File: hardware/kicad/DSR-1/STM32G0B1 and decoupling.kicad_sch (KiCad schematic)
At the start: 0 parts

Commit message: Refactor code structure for improved readability and maintainability
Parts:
- added U5: STM32G0B1KBUx, Package_DFN_QFN:QFN-32-1EP_5x5mm_P0.5mm_EP3.45x3.45mm, symbol DSR-1:STM32G0B1KBUx
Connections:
- net +3.3V: now also U5.1 (PB9), U5.31 (PB7), U5.4 (VDD)
- net GND: now also U5.16 (PB1), U5.17 (PB2), U5.33 (VSS), U5.5 (VSS)

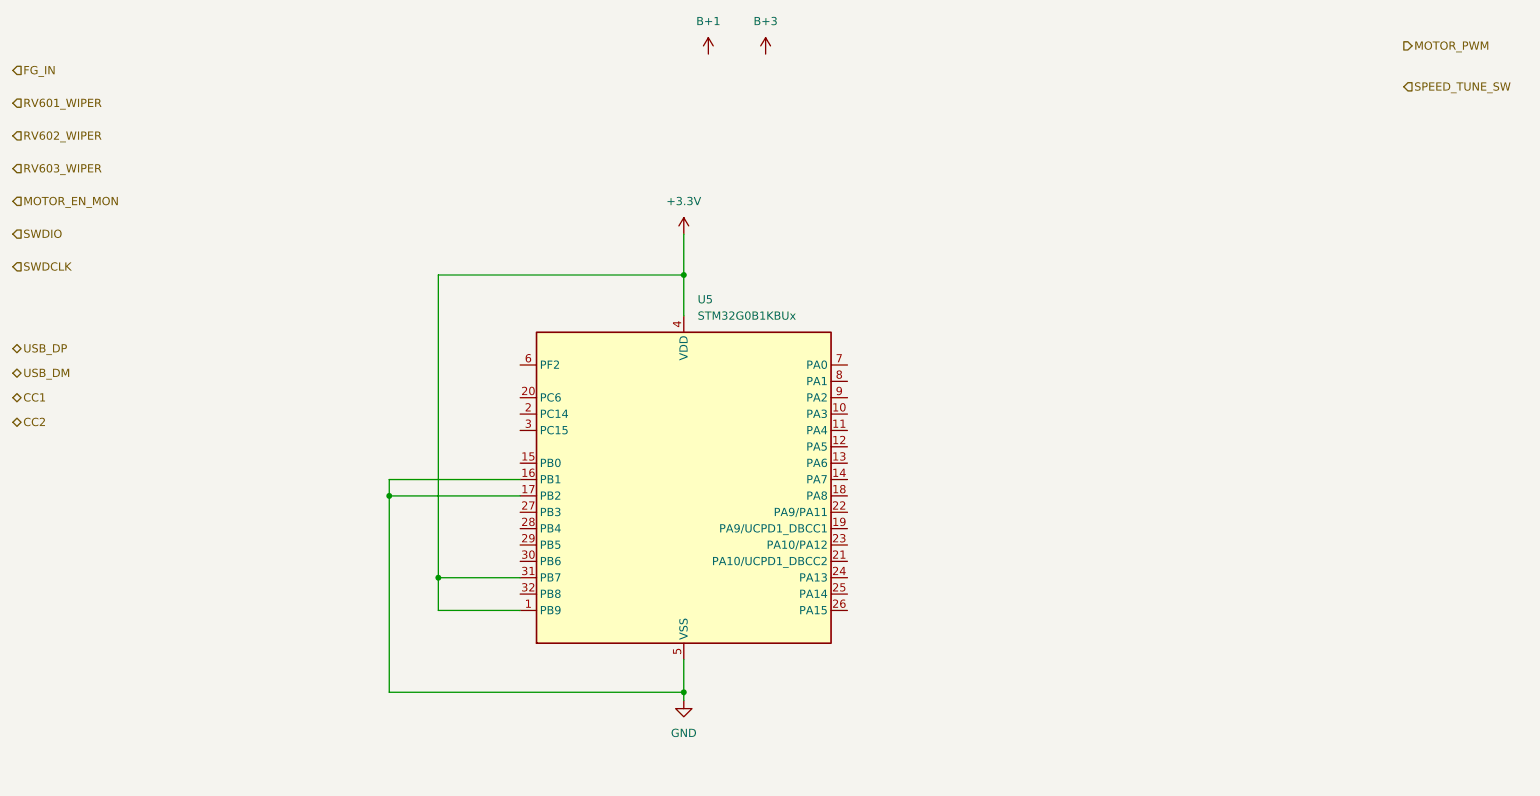
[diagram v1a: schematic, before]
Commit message: Completed microcontroller schematic
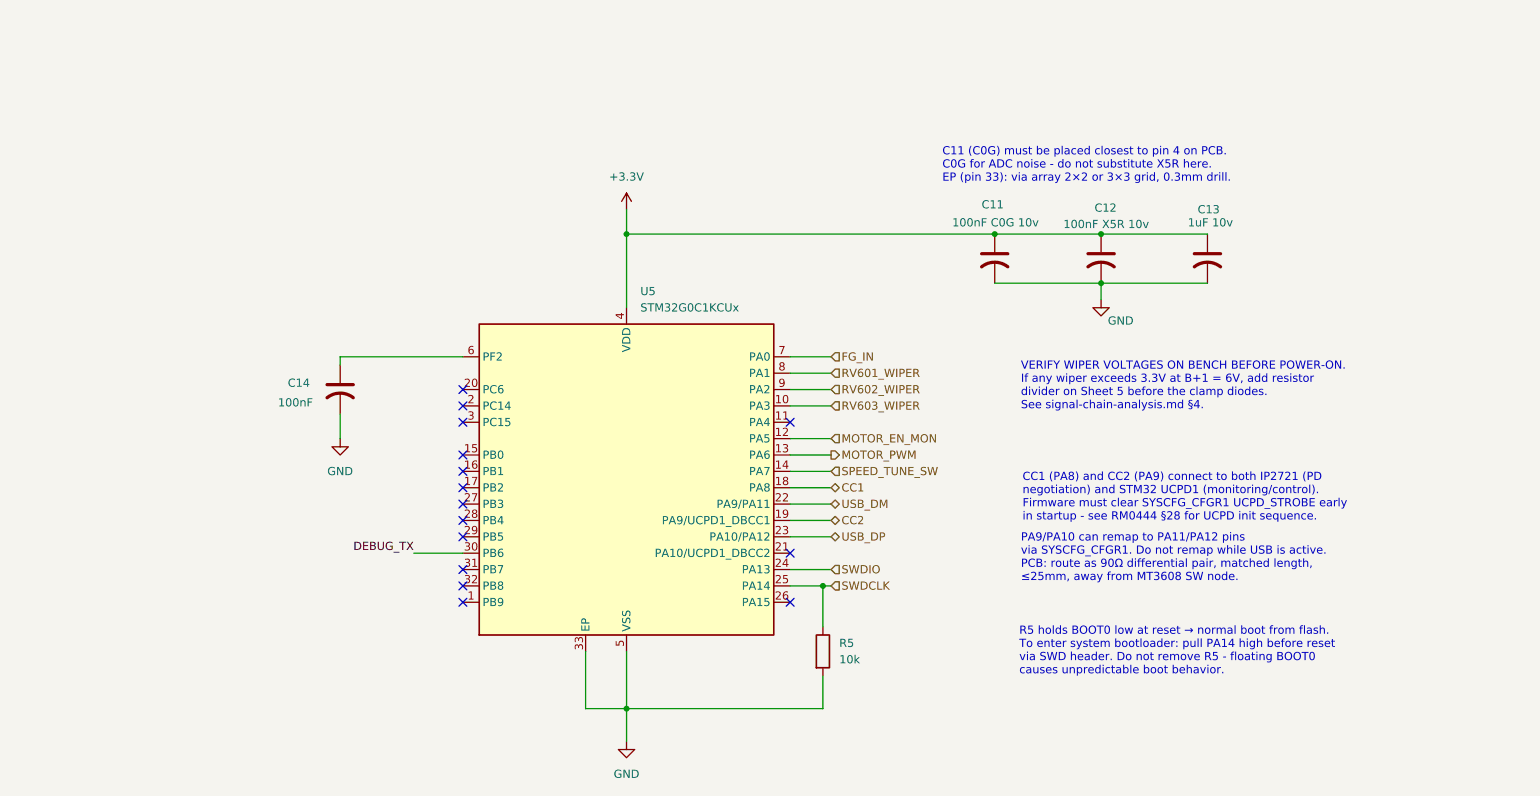
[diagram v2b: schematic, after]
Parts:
- removed U5: STM32G0B1KBUx, Package_DFN_QFN:QFN-32-1EP_5x5mm_P0.5mm_EP3.45x3.45mm, symbol DSR-1:STM32G0B1KBUx
- added C11: 100nF C0G 10v, symbol Device:C_US
- added C12: 100nF X5R 10v, symbol Device:C_US
- added C13: 1uF 10v, symbol Device:C_US
- added C14: 100nF, symbol Device:C_US
- added R5: 10k, symbol Device:R
- added U5: STM32G0C1KCUx, Package_DFN_QFN:QFN-32-1EP_5x5mm_P0.5mm_EP3.45x3.45mm, symbol MCU_ST_STM32G0:STM32G0C1KCUx
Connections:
- net +3.3V: now also C11.1, C12.1, C13.1, U5.4 (VDD)
- net CC1: now also U5.18 (PA8)
- net CC2: now also U5.19 (PA9/UCPD1_DBCC1)
- net FG_IN: now also U5.7 (PA0)
- net GND: now also C11.2, C12.2, C13.2, C14.2, R5.2, U5.33 (VSS), U5.5 (VSS)
- net MOTOR_EN_MON: now also U5.12 (PA5)
- net MOTOR_PWM: now also U5.13 (PA6)
- net RV601_WIPER: now also U5.8 (PA1)
- net RV602_WIPER: now also U5.9 (PA2)
- net RV603_WIPER: now also U5.10 (PA3)
- net SPEED_TUNE_SW: now also U5.14 (PA7)
- net SWDCLK: now also R5.1, U5.25 (PA14)
- net SWDIO: now also U5.24 (PA13)
- net USB_DM: now also U5.22 (PA9/PA11)
- net USB_DP: now also U5.23 (PA10/PA12)
- new net: C14.1, U5.6 (PF2)
- new net DEBUG_TX: U5.30 (PB6)
- no-connect marks 0 -> 15
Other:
- note added: "C11 (C0G) must be placed closest to pin 4 on PCB. C0G for ADC noise - do not substitute X5R here. EP (pin 33): via array 2×2 or 3×3 grid, 0.3mm drill."
- note added: "CC1 (PA8) and CC2 (PA9) connect to both IP2721 (PD negotiation) and STM32 UCPD1 (monitoring/control). Firmware must clear SYSCFG_CFGR1 UCPD_STROBE early in startup - see RM0444 §28 for UCPD init sequence."
- note added: "PA9/PA10 can remap to PA11/PA12 pins via SYSCFG_CFGR1. Do not remap while USB is active. PCB: route as 90Ω differential pair, matched length, ≤25mm, away from MT3608 SW node."
- note added: "R5 holds BOOT0 low at reset → normal boot from flash. To enter system bootloader: pull PA14 high before reset via SWD header. Do not remove R5 - floating BOOT0 causes unpredictable boot behavior."
- note added: "VERIFY WIPER VOLTAGES ON BENCH BEFORE POWER-ON. If any wiper exceeds 3.3V at B+1 = 6V, add resistor divider on Sheet 5 before the clamp diodes. See signal-chain-analysis.md §4."
- title: (none) -> STM32G0C1 and Decoupling
